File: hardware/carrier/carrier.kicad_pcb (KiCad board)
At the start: 2 copper layers, 117.9 x 72.3 mm, 15 parts, among them J1 12V in, U1 D1 Mini ESP32 (Type-C), U2 PCA9685 16ch servo, U3 LM2596 buck 12V->5.05V

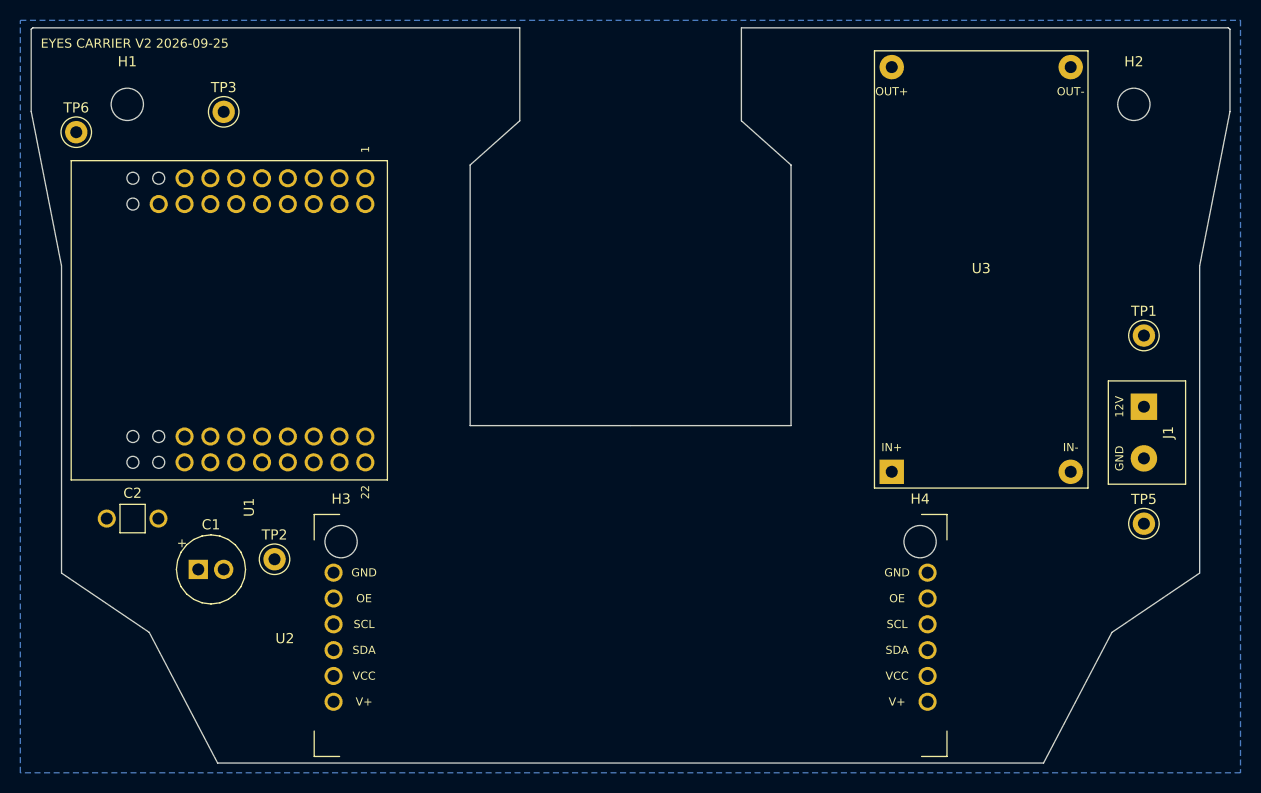
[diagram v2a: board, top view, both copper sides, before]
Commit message: carrier V2: routed single-sided, DRC 0/0/0, mill export + pcbmill drill check passed
All copper is in TRACKS in gen/gen_pcb.py (docstring there is the map). Pin decision:
SDA = IO27 (pad 24), SCL = IO25 (pad 26); firmware needs Wire.begin(27, 25) for the
carrier build (not changed here). IO21/22 are inner-row pins in Scott's placement and
the inner row's only exits are the module's USB end (already carrying +5V and +3V3)
and the antenna end - rejected.

Rejected alternatives, each of which DRC would have accepted:
- I2C to the PCA right row across the front bar: crosses the +3V3 lane.
- +3V3 down the far-left edge: fills the 1.35 mm strip that is GND's only path
  into the D1's middle (pad 33) and the back-left region (TP6).
- Feeding C1.1 by a stub from the y 10.9 run: walled off a GND pocket around C1.2
  that then hung on that pad's spoke alone (KiCad keeps pad-touching pour, so DRC
  says nothing) - now a diagonal off the lane, pour is one polygon + a 2 mm2 sliver.
- A +5V star to pad 35: would cross +3V3 or the GND entries into the left wing;
  V2 is a daisy chain OUT+ -> PCA V+ -> front bar -> left wing -> VCC.

Schematic: I2C nets moved to the PCA left row (3/4), right row keeps +5V/GND; the
jumper_pad_groups make either row valid. Stale V1 routing notes replaced.
export_for_mill.sh: DRC clean, gerbers, one merged drill (3 tools, 71 holes, all
exact bit sizes), annulus gate passed in a throwaway pcbmill job.

Co-Authored-By: Claude Fable 5.1 <noreply@anthropic.com>
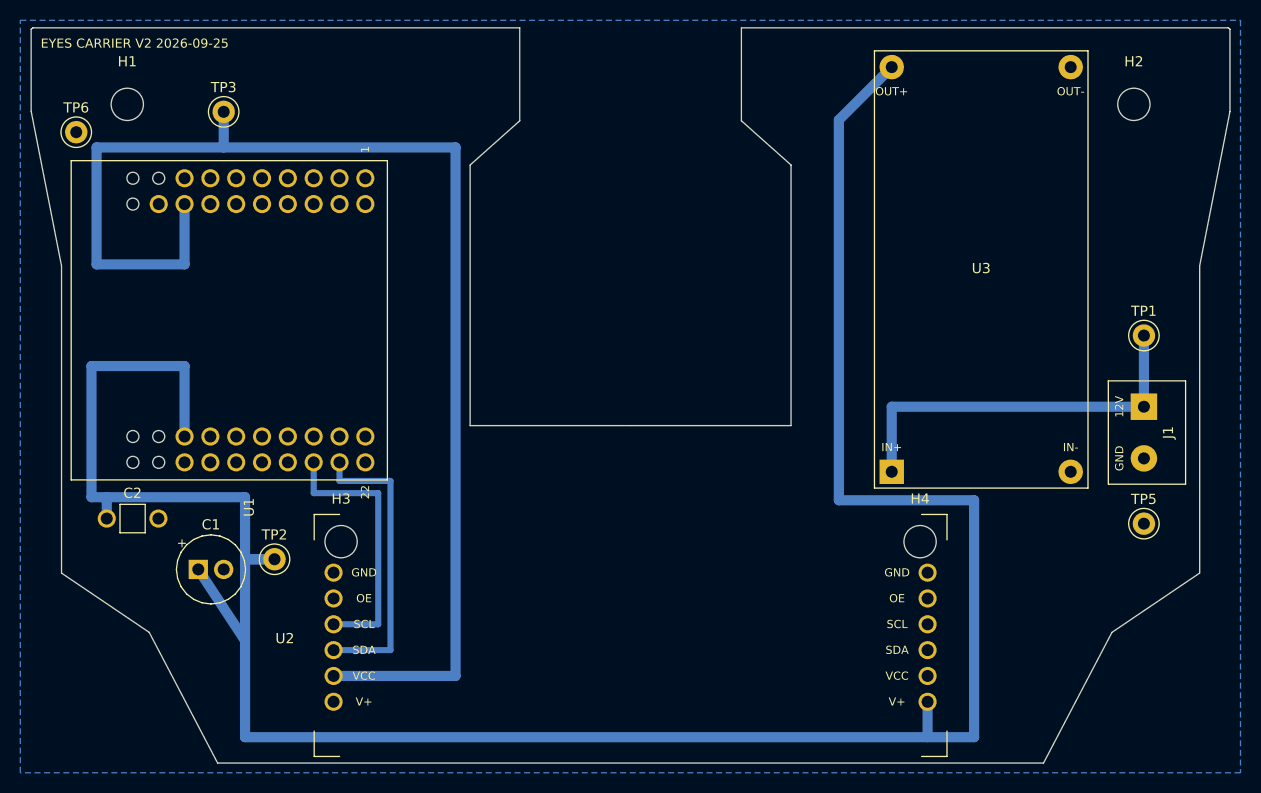
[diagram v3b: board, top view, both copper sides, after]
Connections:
- U1 pad 24: SCL -> SDA
- U1 pad 26: SDA -> SCL
- U2 pad 10: SCL -> (no net)
- U2 pad 3: (no net) -> SDA
- U2 pad 4: (no net) -> SCL
- U2 pad 9: SDA -> (no net)
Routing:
- net +5V: track 0.00 -> 240.5 mm
- net +3V3: track 0.00 -> 128.9 mm
- net +12V: track 0.00 -> 38.2 mm
- net SDA: track 0.00 -> 29.1 mm
- net SCL: track 0.00 -> 26.7 mm
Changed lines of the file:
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@@
 			(layers "*.Cu" "*.Mask")
 			(remove_unused_layers no)
-			(net "SCL")
+			(net "SDA")
 			(thermal_bridge_angle 90)
 		)
@@
 			(layers "*.Cu" "*.Mask")
 			(remove_unused_layers no)
-			(net "SDA")
+			(net "SCL")
 			(thermal_bridge_angle 90)
 		)
@@
 			(layers "*.Cu" "*.Mask")
 			(remove_unused_layers no)
+			(net "SDA")
 			(thermal_bridge_angle 90)
 		)
@@
 			(layers "*.Cu" "*.Mask")
 			(remove_unused_layers no)
+			(net "SCL")
 			(thermal_bridge_angle 90)
 		)
@@
 			(layers "*.Cu" "*.Mask")
 			(remove_unused_layers no)
-			(net "SDA")
 			(thermal_bridge_angle 90)
 		)
@@
 			(layers "*.Cu" "*.Mask")
 			(remove_unused_layers no)
-			(net "SCL")
 			(thermal_bridge_angle 90)
 		)
@@
 		)
 	)
+	(segment
+		(start 47.5 76.5)
+		(end 82.8 76.5)
+		(width 1)
+		(layer "B.Cu")
+		(net "+3V3")
+	)
+	(segment
+		(start 82.8 76.5)
+		(end 82.8 128.478)
+		(width 1)
+		(layer "B.Cu")
+		(net "+3V3")
+	)
+	(segment
+		(start 47.5 88)
+		(end 47.5 76.5)
+		(width 1)
+		(layer "B.Cu")
+		(net "+3V3")
+	)
+	(segment
+		(start 82.8 128.478)
+		(end 70.806 128.478)
+		(width 1)
+		(layer "B.Cu")
+		(net "+3V3")
+	)
+	(segment
+		(start 60 76.5)
+		(end 60 73)
+		(width 1)
+		(layer "B.Cu")
+		(net "+3V3")
+	)
+	(segment
+		(start 56.15 82.07)
+		(end 56.15 88)
+		(width 1)
+		(layer "B.Cu")
+		(net "+3V3")
+	)
+	(segment
+		(start 56.15 88)
+		(end 47.5 88)
+		(width 1)
+		(layer "B.Cu")
+		(net "+3V3")
+	)
+	(segment
+		(start 71.39 107.47)
+		(end 71.39 109.3)
+		(width 0.6)
+		(layer "B.Cu")
+		(net "SDA")
+	)
+	(segment
+		(start 76.4 109.3)
+		(end 76.4 125.938)
+		(width 0.6)
+		(layer "B.Cu")
+		(net "SDA")
+	)
+	(segment
+		(start 76.4 125.938)
+		(end 70.806 125.938)
+		(width 0.6)
+		(layer "B.Cu")
+		(net "SDA")
+	)
+	(segment
+		(start 71.39 109.3)
+		(end 76.4 109.3)
+		(width 0.6)
+		(layer "B.Cu")
+		(net "SDA")
+	)
+	(segment
+		(start 75.2 110.5)
+		(end 75.2 123.398)
+		(width 0.6)
+		(layer "B.Cu")
+		(net "SCL")
+	)
+	(segment
+		(start 75.2 123.398)
+		(end 70.806 123.398)
+		(width 0.6)
+		(layer "B.Cu")
+		(net "SCL")
+	)
+	(segment
+		(start 68.85 107.47)
+		(end 68.85 110.5)
+		(width 0.6)
+		(layer "B.Cu")
+		(net "SCL")
+	)
+	(segment
+		(start 68.85 110.5)
+		(end 75.2 110.5)
+		(width 0.6)
+		(layer "B.Cu")
+		(net "SCL")
+	)
+	(segment
+		(start 120.5 73.8)
+		(end 120.5 111.2)
+		(width 1)
+		(layer "B.Cu")
+		(net "+5V")
+	)
+	(segment
+		(start 133.8 111.2)
+		(end 133.8 134.5)
+		(width 1)
+		(layer "B.Cu")
+		(net "+5V")
+	)
+	(segment
+		(start 62.1 110.9)
+		(end 47 110.9)
+		(width 1)
+		(layer "B.Cu")
+		(net "+5V")
+	)
+	(segment
+		(start 133.8 134.5)
+		(end 62.1 134.5)
+		(width 1)
+		(layer "B.Cu")
+		(net "+5V")
+	)
+	(segment
+		(start 56.15 98)
+		(end 56.15 104.93)
+		(width 1)
+		(layer "B.Cu")
+		(net "+5V")
+	)
+	(segment
+		(start 129.226 134.5)
+		(end 129.226 131.018)
+		(width 1)
+		(layer "B.Cu")
+		(net "+5V")
+	)
+	(segment
+		(start 62.1 125)
+		(end 57.5 118)
+		(width 1)
+		(layer "B.Cu")
+		(net "+5V")
+	)
+	(segment
+		(start 62.1 117)
+		(end 62.1 110.9)
+		(width 1)
+		(layer "B.Cu")
+		(net "+5V")
+	)
+	(segment
+		(start 120.5 111.2)
+		(end 133.8 111.2)
+		(width 1)
+		(layer "B.Cu")
+		(net "+5V")
+	)
+	(segment
+		(start 62.1 134.5)
+		(end 62.1 117)
+		(width 1)
+		(layer "B.Cu")
+		(net "+5V")
+	)
+	(segment
+		(start 125.7 68.6)
+		(end 120.5 73.8)
+		(width 1)
+		(layer "B.Cu")
+		(net "+5V")
+	)
+	(segment
+		(start 47 110.9)
+		(end 47 98)
+		(width 1)
+		(layer "B.Cu")
+		(net "+5V")
+	)
+	(segment
+		(start 65 117)
+		(end 62.1 117)
+		(width 1)
+		(layer "B.Cu")
+		(net "+5V")
+	)
+	(segment
+		(start 47 98)
+		(end 56.15 98)
+		(width 1)
+		(layer "B.Cu")
+		(net "+5V")
+	)
+	(segment
+		(start 48.5 110.9)
+		(end 48.5 113)
+		(width 1)
+		(layer "B.Cu")
+		(net "+5V")
+	)
+	(segment
+		(start 62.1 117)
+		(end 65 117)
+		(width 1)
+		(layer "B.Cu")
+		(net "+5V")
+	)
+	(segment
+		(start 150.5 102)
+		(end 125.7 102)
+		(width 1)
+		(layer "B.Cu")
+		(net "+12V")
+	)
+	(segment
+		(start 125.7 102)
+		(end 125.7 108.4)
+		(width 1)
+		(layer "B.Cu")
+		(net "+12V")
+	)
+	(segment
+		(start 150.5 102)
+		(end 150.5 95)
+		(width 1)
+		(layer "B.Cu")
+		(net "+12V")
+	)
 	(zone
 		(layer "B.Cu")
-		(name "H2 standoff")
+		(name "H4 standoff")
 		(hatch edge 0.5)
 		(connect_pads
@@
 		(polygon
 			(pts
-				(xy 152.763 72.262) (xy 152.652 73.103) (xy 152.328 73.887) (xy 151.811 74.56) (xy 151.138 75.077)
-				(xy 150.354 75.401) (xy 149.513 75.512) (xy 148.672 75.401) (xy 147.888 75.077) (xy 147.215 74.56)
-				(xy 146.698 73.887) (xy 146.374 73.103) (xy 146.263 72.262) (xy 146.374 71.421) (xy 146.698 70.637)
-				(xy 147.215 69.964) (xy 147.888 69.447) (xy 148.672 69.123) (xy 149.513 69.012) (xy 150.354 69.123)
-				(xy 151.138 69.447) (xy 151.811 69.964) (xy 152.328 70.637) (xy 152.652 71.421)
+				(xy 131.737 115.27) (xy 131.626 116.111) (xy 131.302 116.895) (xy 130.785 117.568) (xy 130.112 118.085)
+				(xy 129.328 118.409) (xy 128.487 118.52) (xy 127.646 118.409) (xy 126.862 118.085) (xy 126.189 117.568)
+				(xy 125.672 116.895) (xy 125.348 116.111) (xy 125.237 115.27) (xy 125.348 114.429) (xy 125.672 113.645)
+				(xy 126.189 112.972) (xy 126.862 112.455) (xy 127.646 112.131) (xy 128.487 112.02) (xy 129.328 112.131)
+				(xy 130.112 112.455) (xy 130.785 112.972) (xy 131.302 113.645) (xy 131.626 114.429)
 			)
 		)
@@
 	(zone
 		(layer "B.Cu")
-		(name "H3 standoff")
+		(name "D1 flash pins R")
 		(hatch edge 0.5)
 		(connect_pads
@@
 		(polygon
 			(pts
-				(xy 74.795 115.27) (xy 74.684 116.111) (xy 74.36 116.895) (xy 73.843 117.568) (xy 73.17 118.085)
-				(xy 72.386 118.409) (xy 71.545 118.52) (xy 70.704 118.409) (xy 69.92 118.085) (xy 69.247 117.568)
-				(xy 68.73 116.895) (xy 68.406 116.111) (xy 68.295 115.27) (xy 68.406 114.429) (xy 68.73 113.645)
-				(xy 69.247 112.972) (xy 69.92 112.455) (xy 70.704 112.131) (xy 71.545 112.02) (xy 72.386 112.131)
-				(xy 73.17 112.455) (xy 73.843 112.972) (xy 74.36 113.645) (xy 74.684 114.429)
+				(xy 54.9 103.7) (xy 54.9 108.7) (xy 49.8 108.7) (xy 49.8 103.7)
 			)
 		)
 	)
 	(zone
-		(layer "B.Cu")
-		(name "D1 antenna")
+		(net "GND")
+		(locked yes)
+		(layer "B.Cu")
+		(name "GND pour")
+		(hatch edge 0.5)
+		(connect_pads thru_hole_only
+			(clearance 0.6)
+		)
+		(min_thickness 0.5)
+		(fill yes
+			(thermal_gap 0.5)
+			(thermal_bridge_width 0.5)
+			(island_removal_mode 0)
+		)
+		(polygon
+			(pts
+				(xy 40 64) (xy 160 64) (xy 160 138) (xy 40 138)
+			)
+		)
+	)
+	(zone
+		(layer "B.Cu")
+		(name "H2 standoff")
 		(hatch edge 0.5)
 		(connect_pads
@@
 		(polygon
 			(pts
-				(xy 82 77.8) (xy 82 109.2) (xy 73.93 109.2) (xy 73.93 77.8)
+				(xy 152.763 72.262) (xy 152.652 73.103) (xy 152.328 73.887) (xy 151.811 74.56) (xy 151.138 75.077)
+				(xy 150.354 75.401) (xy 149.513 75.512) (xy 148.672 75.401) (xy 147.888 75.077) (xy 147.215 74.56)
+				(xy 146.698 73.887) (xy 146.374 73.103) (xy 146.263 72.262) (xy 146.374 71.421) (xy 146.698 70.637)
+				(xy 147.215 69.964) (xy 147.888 69.447) (xy 148.672 69.123) (xy 149.513 69.012) (xy 150.354 69.123)
+				(xy 151.138 69.447) (xy 151.811 69.964) (xy 152.328 70.637) (xy 152.652 71.421)
 			)
 		)
@@
 	(zone
 		(layer "B.Cu")
-		(name "D1 flash pins R")
+		(name "H3 standoff")
 		(hatch edge 0.5)
 		(connect_pads
@@
 		(polygon
 			(pts
-				(xy 54.9 103.7) (xy 54.9 108.7) (xy 49.8 108.7) (xy 49.8 103.7)
-			)
-		)
-	)
-	(zone
-		(net "GND")
-		(locked yes)
-		(layer "B.Cu")
-		(name "GND pour")
-		(hatch edge 0.5)
-		(connect_pads thru_hole_only
-			(clearance 0.6)
-		)
-		(min_thickness 0.5)
-		(fill yes
-			(thermal_gap 0.5)
-			(thermal_bridge_width 0.5)
-			(island_removal_mode 0)
-		)
-		(polygon
-			(pts
-				(xy 40 64) (xy 160 64) (xy 160 138) (xy 40 138)
+				(xy 74.795 115.27) (xy 74.684 116.111) (xy 74.36 116.895) (xy 73.843 117.568) (xy 73.17 118.085)
+				(xy 72.386 118.409) (xy 71.545 118.52) (xy 70.704 118.409) (xy 69.92 118.085) (xy 69.247 117.568)
+				(xy 68.73 116.895) (xy 68.406 116.111) (xy 68.295 115.27) (xy 68.406 114.429) (xy 68.73 113.645)
+				(xy 69.247 112.972) (xy 69.92 112.455) (xy 70.704 112.131) (xy 71.545 112.02) (xy 72.386 112.131)
+				(xy 73.17 112.455) (xy 73.843 112.972) (xy 74.36 113.645) (xy 74.684 114.429)
 			)
 		)
@@
 	(zone
 		(layer "B.Cu")
-		(name "H4 standoff")
+		(name "D1 antenna")
 		(hatch edge 0.5)
 		(connect_pads
@@
 		(polygon
 			(pts
-				(xy 131.737 115.27) (xy 131.626 116.111) (xy 131.302 116.895) (xy 130.785 117.568) (xy 130.112 118.085)
-				(xy 129.328 118.409) (xy 128.487 118.52) (xy 127.646 118.409) (xy 126.862 118.085) (xy 126.189 117.568)
-				(xy 125.672 116.895) (xy 125.348 116.111) (xy 125.237 115.27) (xy 125.348 114.429) (xy 125.672 113.645)
-				(xy 126.189 112.972) (xy 126.862 112.455) (xy 127.646 112.131) (xy 128.487 112.02) (xy 129.328 112.131)
-				(xy 130.112 112.455) (xy 130.785 112.972) (xy 131.302 113.645) (xy 131.626 114.429)
-			)
-		)
+				(xy 82 77.8) (xy 82 109.2) (xy 73.93 109.2) (xy 73.93 77.8)
+			)
+		)
